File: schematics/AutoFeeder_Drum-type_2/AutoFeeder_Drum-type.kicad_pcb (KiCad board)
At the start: 2 copper layers, 32 x 70 mm, 54 parts, among them J1 USB_C_Receptacle_6, J2 Conn_01x05, J3 Conn_02x02_Odd_Even, J4 Conn_02x03_Odd_Even, J5 Conn_01x01, J6 Conn_01x01, J7 Conn_01x04, M1 Motor_DC, SW1 TMHU26, U1 CNZ1023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

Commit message: Two types of sensors CNZ1023 and NJL5901 are supported. When the center button is pressed and held for 2 seconds, the hole position is memorized for one revolution, then returns to the original position. Circuit diagram is in the process of modification.
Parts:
- removed J1: USB_C_Receptacle_6, mylib:USB_C_6
- removed R1, R2: 5.1k, Resistor_SMD:R_0603_1608Metric
- moved J5 51.2 mm to (114.0, 126.9)
- moved J6 51.2 mm to (114.0, 134.5)
- moved REF** 51.2 mm to (117.8, 130.7)
- moved U1 51.2 mm to (121.6, 129.4)
- moved C2 1.91 mm to (114.0, 107.3)
- moved J2 1.27 mm to (105.2, 122.6)
- moved JP1 1.27 mm to (107.8, 125.7)
- moved R8 1.27 mm to (108.9, 113.0)
- moved U7 1.25 mm to (114.0, 114.9)
- moved C1 1.03 mm to (106.0, 111.1)
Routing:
- net GND: track 68.0 -> 60.0 mm, vias 10 -> 8
- net Net-(J1-CC1): track 4.14 -> 0.00 mm
- net Net-(J1-CC2): track 3.66 -> 0.00 mm
- net Net-(J2-Pin_2): track 25.8 -> 28.9 mm
- net /RA4: track 13.5 -> 14.7 mm
- net /FWD: track 19.7 -> 20.9 mm
- net /CCW: track 44.7 -> 45.3 mm
- net /REV: track 19.7 -> 20.2 mm
- net /CW: track 28.0 -> 28.5 mm

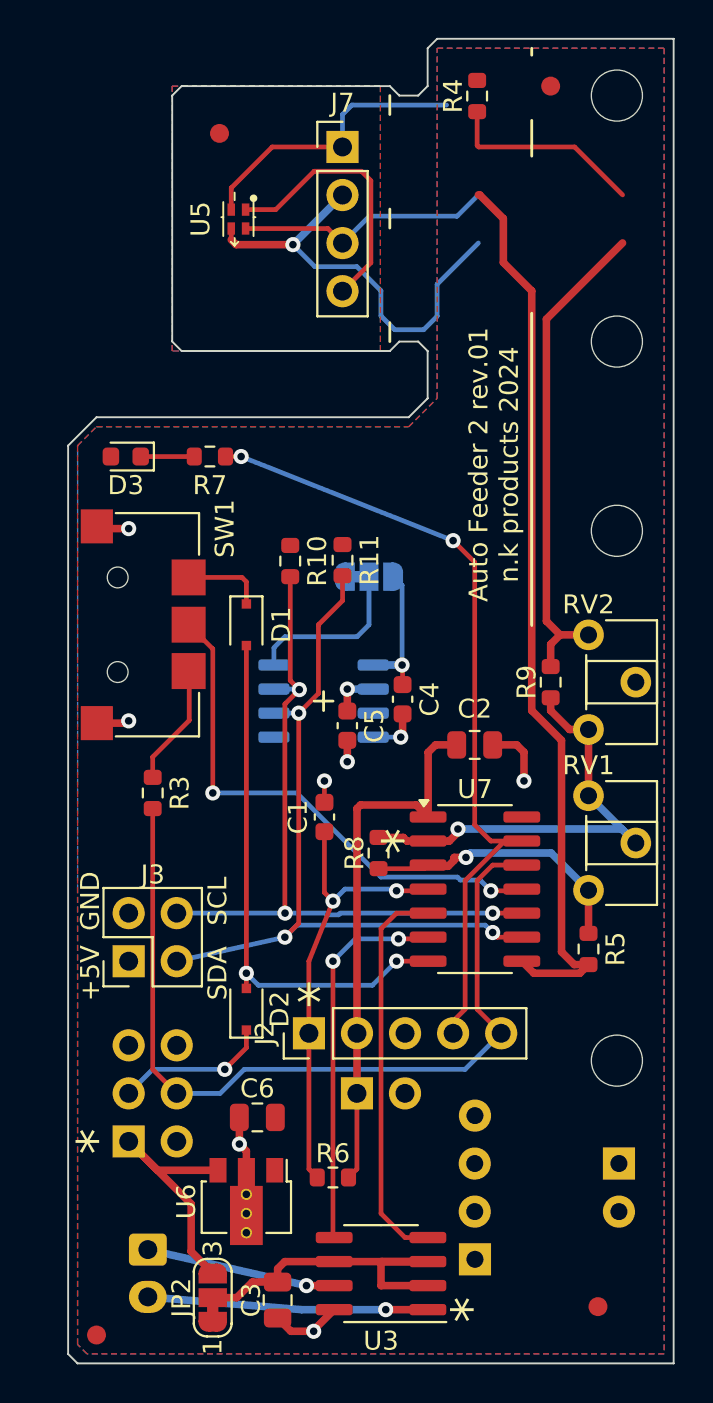
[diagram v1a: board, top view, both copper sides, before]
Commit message: Auto Feeder 2 rev.1 ; The board is placed vertically to save space. Transmissive photo interrupter CNZ1023 can also be used.
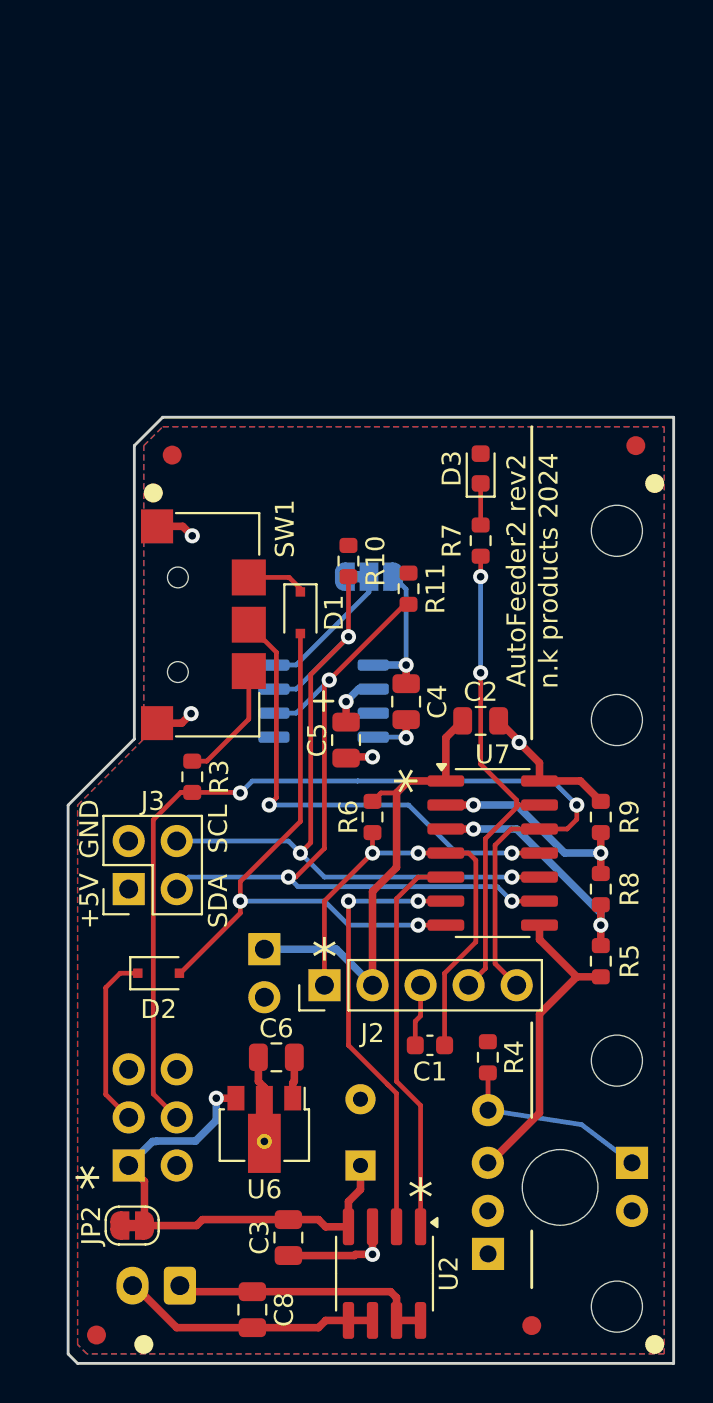
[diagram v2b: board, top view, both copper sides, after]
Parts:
- removed the ? at (101.9, 131.1)
- removed Fid2: Fiducial_1mm_Mask3mm, Fiducial:Fiducial_1mm_Mask3mm
- removed J7: Conn_01x04, Connector_PinHeader_2.54mm:PinHeader_1x04_P2.54mm_Vertical
- removed the REF** at (110.5, 82.5)
- removed the REF** at (121.5, 73.0)
- removed the REF** at (121.5, 86.0)
- removed the REF** at (101.9, 133.1)
- removed the REF** at (110.5, 76.5)
- removed the REF** at (117.8, 130.7)
- removed RV1, RV2: 20k, Potentiometer_THT:Potentiometer_ACP_CA6-H2,5_Horizontal
- removed U3: ZXBM5210-S, Package_SO:SOIC-8_3.9x4.9mm_P1.27mm
- removed U5: NJL5901AR-1, mylib:NJL5901AR-1
- added C7: 220uF, Capacitor_THT:CP_Radial_D8.0mm_P3.50mm, B.Cu at (108.0, 129.5)
- added C8: 0.1uF, Capacitor_SMD:C_0805_2012Metric, F.Cu at (102.2, 137.2)
- added Fed2: Fiducial_1mm_Mask3mm, Fiducial:Fiducial_1mm_Mask3mm, F.Cu at (98.0, 92.0)
- added Fid5: Fiducial_Silk, mylib:Fiducial_Silk, F.Cu at (96.5, 139.0)
- added Fid6: Fiducial_Silk, mylib:Fiducial_Silk, F.Cu at (97.0, 94.0)
- added Fid7: Fiducial_Silk, mylib:Fiducial_Silk, F.Cu at (123.5, 93.5)
- added Fid8: Fiducial_Silk, mylib:Fiducial_Silk, F.Cu at (123.5, 139.0)
- added REF**: MountingHole_2.7mm_M2.5, MountingHole:MountingHole_2.7mm_M2.5, F.Cu at (121.5, 137.0)
- added REF**: DrillHole5mm, mylib:DrillHole5mm, F.Cu at (118.5, 130.7)
- added REF**: MountingHole_2.7mm_M2.5, MountingHole:MountingHole_2.7mm_M2.5, F.Cu at (121.5, 106.0)
- added U2: AM2837, Package_SO:SOIC-8_3.9x4.9mm_P1.27mm, F.Cu at (109.2, 135.3)
- C3: value 10u -> 0.1uF
- C4, C5: footprint Capacitor_SMD:C_0603_1608Metric -> Capacitor_SMD:C_0805_2012Metric
- JP2: value SolderJumper_3_Bridged12 -> SolderJumper_2_Bridged; footprint Jumper:SolderJumper-3_P1.3mm_Bridged12_RoundedPad1.0x1.5mm_NumberLabels -> Jumper:SolderJumper-2_P1.3mm_Bridged_RoundedPad1.0x1.5mm
- moved R4 50.8 mm to (114.7, 123.8)
- moved Fed3 19.5 mm to (122.5, 91.5)
- moved R6 19.2 mm to (108.6, 111.1), turned to 90 degrees
- moved D3 18.8 mm to (114.3, 92.7), turned to 90 degrees
- moved R7 15.0 mm to (114.3, 96.5), turned to -90 degrees
- moved C1 13.3 mm to (111.6, 123.2), turned to 180 degrees
- moved R8 11.9 mm to (120.7, 114.9)
- moved JP1 9.06 mm to (102.9, 118.1), turned to 180 degrees
- moved R9 7.60 mm to (120.7, 111.1)
- moved JP2 5.71 mm to (95.9, 132.7), turned to 180 degrees
- moved D2 5.01 mm to (97.3, 119.4), turned to 0 degrees
- moved ? 3.93 mm to (102.9, 128.3)
- moved U6 3.93 mm to (102.9, 127.6)
- moved J3 3.81 mm to (95.7, 114.9)
- moved R11 3.80 mm to (110.5, 99.1)
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- renumbered REF** to Fed1
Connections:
- C3 pad 1: Net-(JP2-C) -> Net-(J4-Pin_1)
- JP2 pad 1: +5V -> Net-(J4-Pin_1)
- JP2 pad 2: Net-(JP2-C) -> +5V
- M1 pad 1: /M2 -> /M1
- M1 pad 2: /M1 -> /M2
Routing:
- net /Sensor0: track 61.2 -> 16.7 mm
- net GND: track 60.0 -> 27.6 mm, vias 8 -> 6
- net +5V: track 30.4 -> 10.1 mm, vias 2 -> 1
- net Net-(JP2-C): track 18.8 -> 0.00 mm
- net Net-(J2-Pin_4): track 43.4 -> 25.7 mm
- net Net-(J7-Pin_4): track 14.1 -> 0.00 mm
- net /RA5: track 24.5 -> 11.4 mm, vias 1 -> 2
- net Net-(J4-Pin_1): track 14.1 -> 25.9 mm, vias 0 -> 1
- net /CCW: track 45.3 -> 53.5 mm, vias 0 -> 2
- net Net-(J2-Pin_2): track 28.9 -> 25.1 mm
- net /M2: track 10.1 -> 13.8 mm, vias 1 -> 0
- net /CW: track 28.5 -> 32.0 mm
- net /REV: track 20.2 -> 23.4 mm
- net /SCL: track 38.0 -> 40.7 mm
- net /RA2: track 27.9 -> 25.6 mm
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- removed copper zone on F.Cu, net GND
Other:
- board size 32 x 70 mm -> 32 x 50 mm
- rule pad_to_mask_clearance: 0 -> 0.038
- board text added: "AutoFeeder2 rev2"
- board text added: "n.k products 2024"
- board text removed: "Auto Feeder 2 rev.01 n.k products 2024"
